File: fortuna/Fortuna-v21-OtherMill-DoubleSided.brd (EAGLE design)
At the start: 66 x 55.9 mm, 41 parts, among them IC1 OPA4340P, J1 5V, J2 GND, J3 A0, J4 A3, J5 A5, J6 D2, J7 *D5, J8 *D10, J9 VIN, M1 MOTOR20MM, M2 MOTOR20MM, Q1 PN2222A, Q2 PN2222A

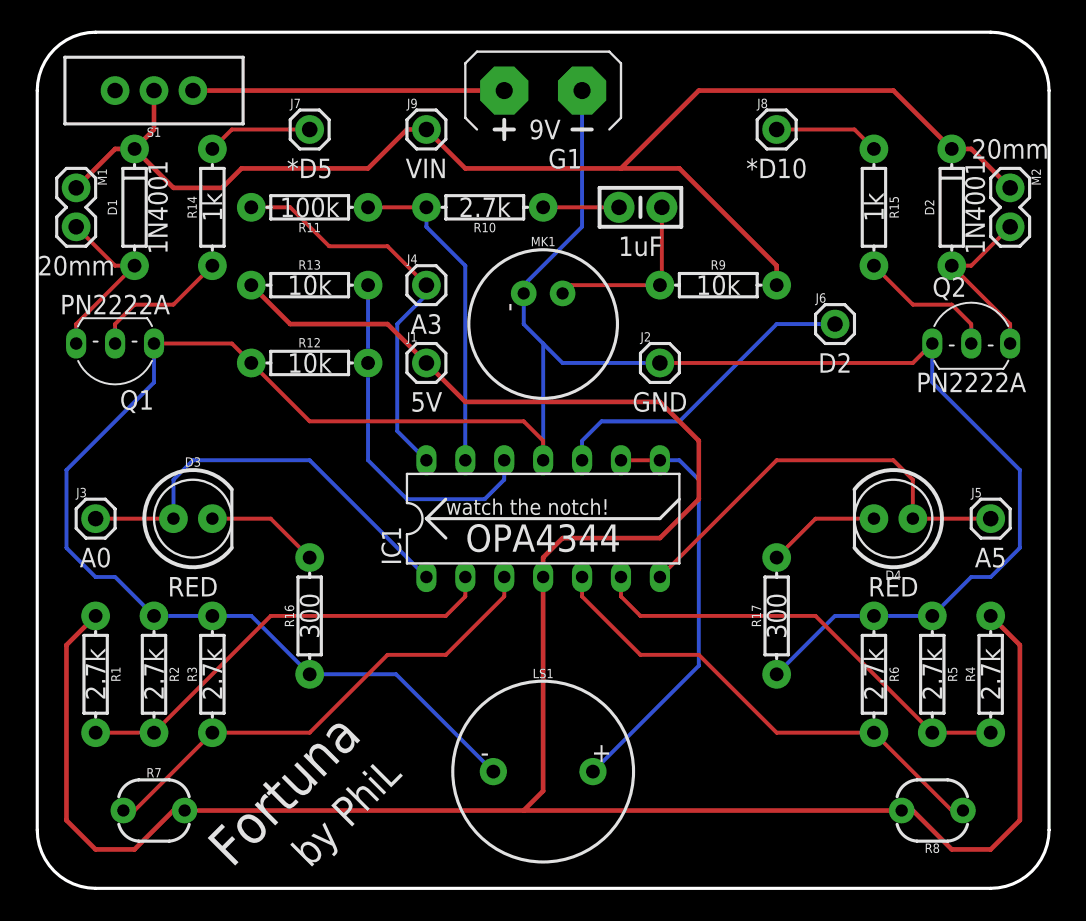
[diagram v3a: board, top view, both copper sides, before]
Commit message: Change trace widths (See description)
netclass power: width = 0.018" = 18 mil
netclass default: width = 0.016" = 16 mil
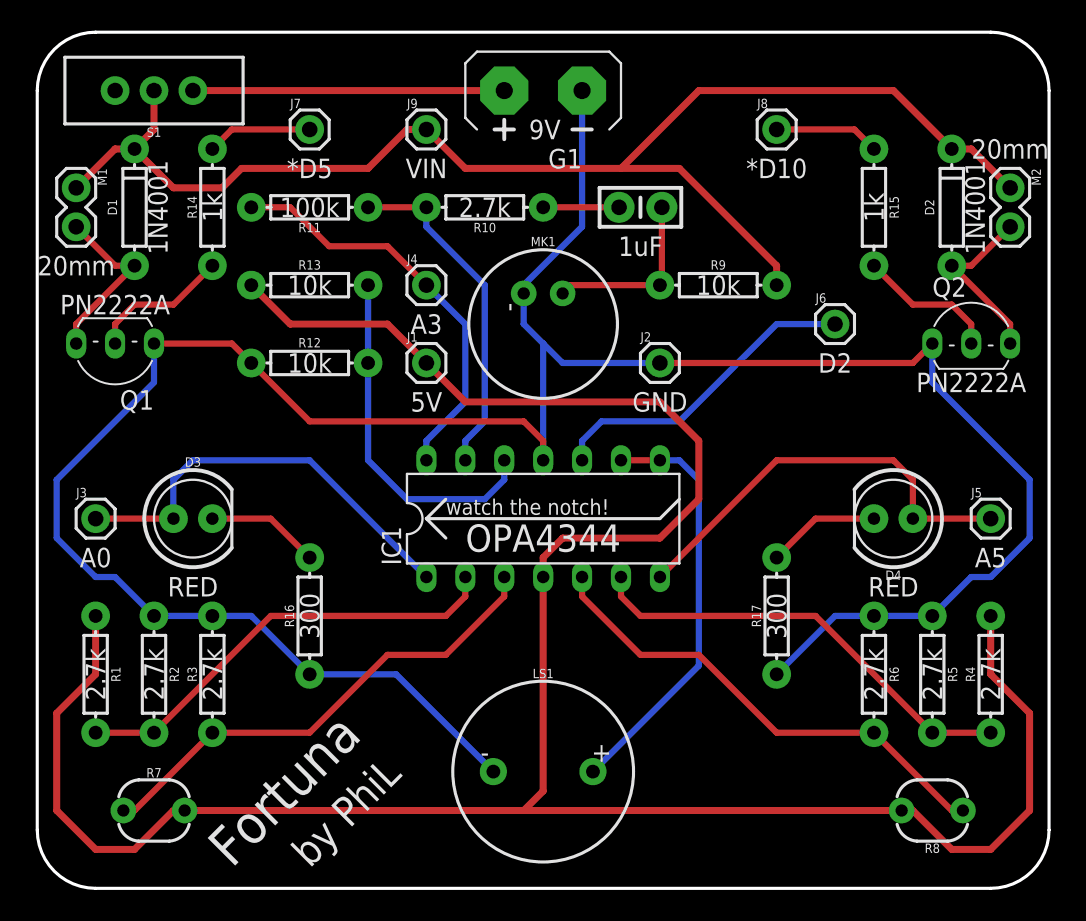
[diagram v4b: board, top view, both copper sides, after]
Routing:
- net OUT_MIC: track 26.5 -> 27.7 mm
- net -MIC: track 21.4 -> 22.4 mm
- net GND: track 166.6 -> 167.7 mm
- net 5V: track 160.2 -> 161.2 mm
